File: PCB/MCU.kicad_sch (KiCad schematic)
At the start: 28 parts, among them J1 SWD, SW65 USB Boot, SW66 Reset, U2 W25Q128JVS, U3 RP2040, Y1 12MHz

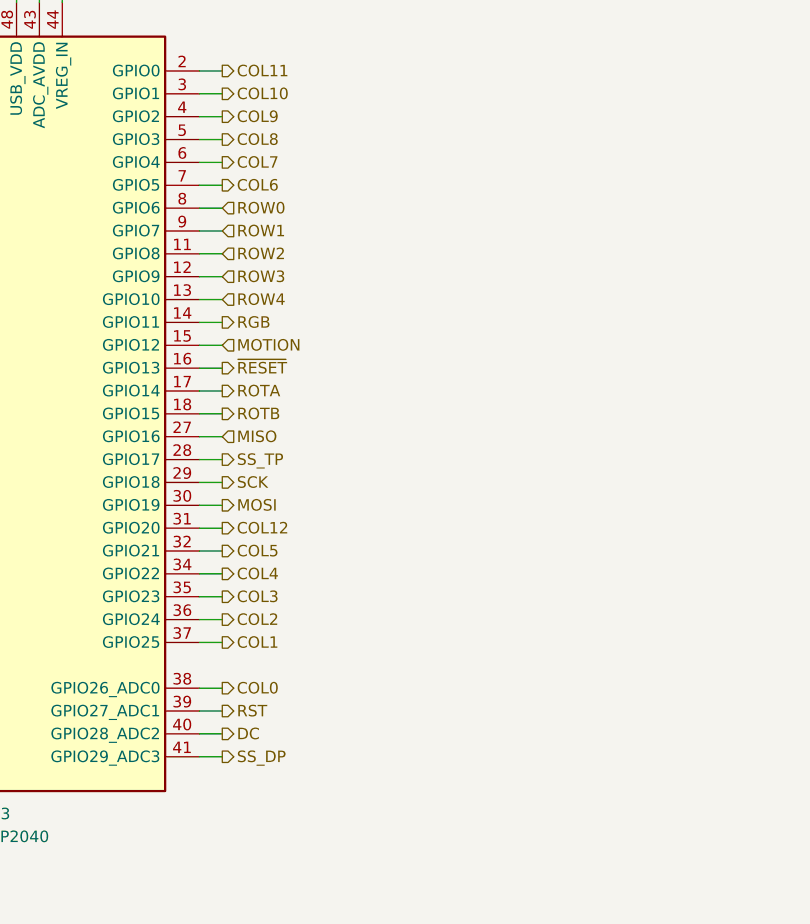
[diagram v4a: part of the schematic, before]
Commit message: Added level shifter to the RGB signal, just in case.
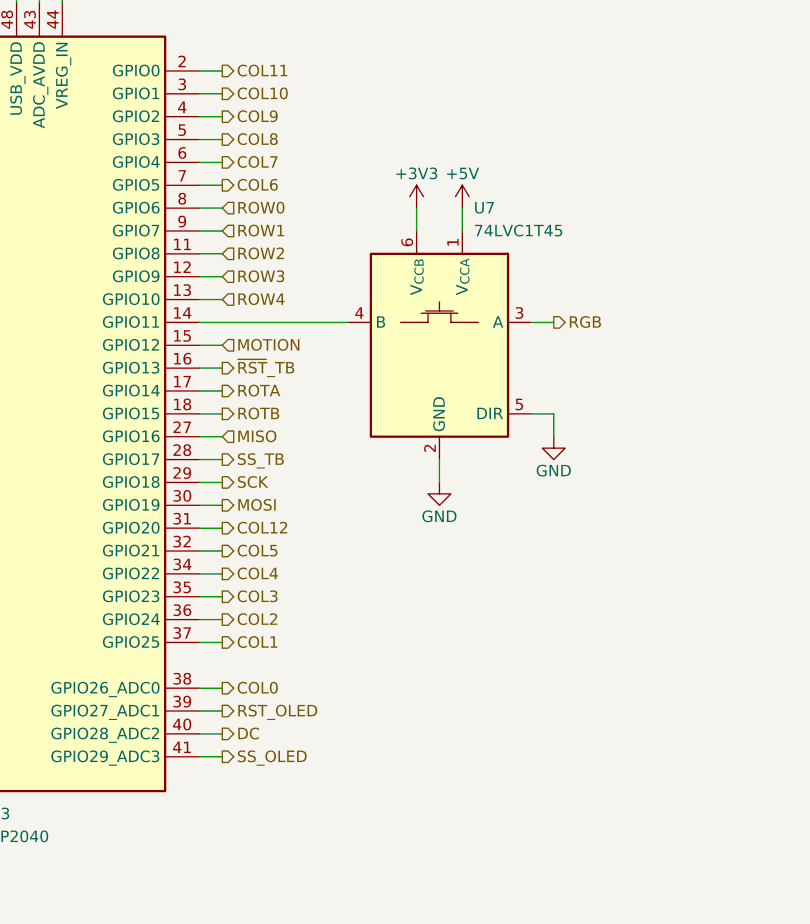
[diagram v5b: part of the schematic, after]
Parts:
- added U7: 74LVC1T45, Package_TO_SOT_SMD:SOT-363_SC-70-6, symbol Cantaloupe:74LVC1T45
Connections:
- net +3V3: now also U7.6 (V_{CCB})
- net GND: now also U7.2 (GND), U7.5 (DIR)
- net RGB: now also U7.3 (A); no longer U3.14 (GPIO11)
- net RST renamed RST_OLED
- net SS_DP renamed SS_OLED
- net SS_TP renamed SS_TB
- net ~{RESET} renamed ~{RST}_TB
- new net: U3.14 (GPIO11), U7.4 (B)
- new net +5V: U7.1 (V_{CCA})
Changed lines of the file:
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@@
 (kicad_sch (version 20230121) (generator eeschema)
   (paper "A4")
+  (title_block
+    (date "2023-03-18")
+    (rev "V1.1")
+  )
   (junction (at 132.08 31.75) (diameter 0) (color 0 0 0 0)
   )
@@
     (stroke (width 0) (type default))
   )
+  (wire (pts (xy 114.3 86.36) (xy 130.81 86.36))
+    (stroke (width 0) (type default))
+  )
   (wire (pts (xy 193.04 31.75) (xy 193.04 34.29))
     (stroke (width 0) (type default))
@@
     (stroke (width 0) (type default))
   )
+  (wire (pts (xy 143.51 73.66) (xy 143.51 76.2))
+    (stroke (width 0) (type default))
+  )
+  (wire (pts (xy 138.43 73.66) (xy 138.43 76.2))
+    (stroke (width 0) (type default))
+  )
   (wire (pts (xy 60.96 129.54) (xy 60.96 127))
     (stroke (width 0) (type default))
@@
     (stroke (width 0) (type default))
   )
+  (wire (pts (xy 153.67 96.52) (xy 151.13 96.52))
+    (stroke (width 0) (type default))
+  )
   (wire (pts (xy 152.4 29.21) (xy 152.4 31.75))
     (stroke (width 0) (type default))
@@
     (stroke (width 0) (type default))
   )
-  (wire (pts (xy 114.3 86.36) (xy 116.84 86.36))
-    (stroke (width 0) (type default))
-  )
   (wire (pts (xy 142.24 31.75) (xy 132.08 31.75))
     (stroke (width 0) (type default))
@@
     (stroke (width 0) (type default))
   )
+  (wire (pts (xy 140.97 101.6) (xy 140.97 104.14))
+    (stroke (width 0) (type default))
+  )
   (wire (pts (xy 45.72 114.3) (xy 48.26 114.3))
     (stroke (width 0) (type default))
@@
     (stroke (width 0) (type default))
   )
+  (wire (pts (xy 151.13 86.36) (xy 153.67 86.36))
+    (stroke (width 0) (type default))
+  )
   (wire (pts (xy 132.08 31.75) (xy 121.92 31.75))
     (stroke (width 0) (type default))
@@
   )
   (wire (pts (xy 162.56 21.59) (xy 162.56 24.13))
+    (stroke (width 0) (type default))
+  )
+  (wire (pts (xy 153.67 99.06) (xy 153.67 96.52))
     (stroke (width 0) (type default))
   )
@@
     (effects (font (size 1.27 1.27)) (justify left))
   )
-  (hierarchical_label "RGB" (shape output) (at 116.84 86.36 0) (fields_autoplaced)
-    (effects (font (size 1.27 1.27)) (justify left))
-  )
   (hierarchical_label "D+" (shape input) (at 53.34 66.04 180) (fields_autoplaced)
     (effects (font (size 1.27 1.27)) (justify right))
   )
-  (hierarchical_label "RST" (shape output) (at 116.84 129.54 0) (fields_autoplaced)
+  (hierarchical_label "SS_TB" (shape output) (at 116.84 101.6 0) (fields_autoplaced)
     (effects (font (size 1.27 1.27)) (justify left))
   )
@@
     (effects (font (size 1.27 1.27)) (justify left))
   )
-  (hierarchical_label "SS_TP" (shape output) (at 116.84 101.6 0) (fields_autoplaced)
-    (effects (font (size 1.27 1.27)) (justify left))
-  )
   (hierarchical_label "ROTB" (shape output) (at 116.84 96.52 0) (fields_autoplaced)
     (effects (font (size 1.27 1.27)) (justify left))
@@
     (effects (font (size 1.27 1.27)) (justify left))
   )
-  (hierarchical_label "~{RESET}" (shape output) (at 116.84 91.44 0) (fields_autoplaced)
-    (effects (font (size 1.27 1.27)) (justify left))
-  )
   (hierarchical_label "ROW4" (shape input) (at 116.84 83.82 0) (fields_autoplaced)
     (effects (font (size 1.27 1.27)) (justify left))
   )
-  (hierarchical_label "SS_DP" (shape output) (at 116.84 134.62 0) (fields_autoplaced)
-    (effects (font (size 1.27 1.27)) (justify left))
-  )
   (hierarchical_label "SCK" (shape output) (at 116.84 104.14 0) (fields_autoplaced)
     (effects (font (size 1.27 1.27)) (justify left))
@@
     (effects (font (size 1.27 1.27)) (justify left))
   )
+  (hierarchical_label "RST_OLED" (shape output) (at 116.84 129.54 0) (fields_autoplaced)
+    (effects (font (size 1.27 1.27)) (justify left))
+  )
   (hierarchical_label "COL12" (shape output) (at 116.84 109.22 0) (fields_autoplaced)
     (effects (font (size 1.27 1.27)) (justify left))
@@
     (effects (font (size 1.27 1.27)) (justify left))
   )
+  (hierarchical_label "RGB" (shape output) (at 153.67 86.36 0) (fields_autoplaced)
+    (effects (font (size 1.27 1.27)) (justify left))
+  )
+  (hierarchical_label "~{RST}_TB" (shape output) (at 116.84 91.44 0) (fields_autoplaced)
+    (effects (font (size 1.27 1.27)) (justify left))
+  )
   (hierarchical_label "COL5" (shape output) (at 116.84 111.76 0) (fields_autoplaced)
+    (effects (font (size 1.27 1.27)) (justify left))
+  )
+  (hierarchical_label "SS_OLED" (shape output) (at 116.84 134.62 0) (fields_autoplaced)
     (effects (font (size 1.27 1.27)) (justify left))
   )
@@
     )
   )
+  (symbol (lib_id "power:GND") (at 140.97 104.14 0) (unit 1)
+    (in_bom yes) (on_board yes) (dnp no)
+    (property "Reference" "#PWR056" (at 140.97 110.49 0)
+      (effects (font (size 1.27 1.27)) hide)
+    )
+    (property "Value" "GND" (at 140.97 107.95 0)
+      (effects (font (size 1.27 1.27)))
+    )
+    (property "Footprint" "" (at 140.97 104.14 0)
+      (effects (font (size 1.27 1.27)) hide)
+    )
+    (property "Datasheet" "" (at 140.97 104.14 0)
+      (effects (font (size 1.27 1.27)) hide)
+    )
+    (pin "1")
+    (instances
+      (project "Honeydew"
+        (path "/534caec7-cf60-4f90-b1ed-42c9d445ef0f/d133c1c6-f35d-4b98-81a0-3607ab1d2de1"
+          (reference "#PWR056") (unit 1)
+        )
+      )
+    )
+  )
   (symbol (lib_id "Connector_Generic:Conn_01x04") (at 50.8 127 180) (unit 1)
     (in_bom no) (on_board yes) (dnp no) (fields_autoplaced)
@@
     )
   )
+  (symbol (lib_id "power:+5V") (at 143.51 73.66 0) (unit 1)
+    (in_bom yes) (on_board yes) (dnp no) (fields_autoplaced)
+    (property "Reference" "#PWR057" (at 143.51 77.47 0)
+      (effects (font (size 1.27 1.27)) hide)
+    )
+    (property "Value" "+5V" (at 143.51 69.85 0)
+      (effects (font (size 1.27 1.27)))
+    )
+    (property "Footprint" "" (at 143.51 73.66 0)
+      (effects (font (size 1.27 1.27)) hide)
+    )
+    (property "Datasheet" "" (at 143.51 73.66 0)
+      (effects (font (size 1.27 1.27)) hide)
+    )
+    (pin "1")
+    (instances
+      (project "Honeydew"
+        (path "/534caec7-cf60-4f90-b1ed-42c9d445ef0f/d133c1c6-f35d-4b98-81a0-3607ab1d2de1"
+          (reference "#PWR057") (unit 1)
+        )
+      )
+    )
+  )
   (symbol (lib_id "Cantaloupe:SW_SPST_Small") (at 55.88 58.42 0) (unit 1)
     (in_bom yes) (on_board yes) (dnp no) (fields_autoplaced)
@@
     )
   )
+  (symbol (lib_id "power:+3V3") (at 138.43 73.66 0) (unit 1)
+    (in_bom yes) (on_board yes) (dnp no) (fields_autoplaced)
+    (property "Reference" "#PWR055" (at 138.43 77.47 0)
+      (effects (font (size 1.27 1.27)) hide)
+    )
+    (property "Value" "+3V3" (at 138.43 69.85 0)
+      (effects (font (size 1.27 1.27)))
+    )
+    (property "Footprint" "" (at 138.43 73.66 0)
+      (effects (font (size 1.27 1.27)) hide)
+    )
+    (property "Datasheet" "" (at 138.43 73.66 0)
+      (effects (font (size 1.27 1.27)) hide)
+    )
+    (pin "1")
+    (instances
+      (project "Honeydew"
+        (path "/534caec7-cf60-4f90-b1ed-42c9d445ef0f/d133c1c6-f35d-4b98-81a0-3607ab1d2de1"
+          (reference "#PWR055") (unit 1)
+        )
+      )
+    )
+  )
   (symbol (lib_id "power:GND") (at 53.34 48.26 0) (unit 1)
     (in_bom yes) (on_board yes) (dnp no)
@@
     )
   )
+  (symbol (lib_id "power:GND") (at 153.67 99.06 0) (unit 1)
+    (in_bom yes) (on_board yes) (dnp no)
+    (property "Reference" "#PWR017" (at 153.67 105.41 0)
+      (effects (font (size 1.27 1.27)) hide)
+    )
+    (property "Value" "GND" (at 153.67 102.87 0)
+      (effects (font (size 1.27 1.27)))
+    )
+    (property "Footprint" "" (at 153.67 99.06 0)
+      (effects (font (size 1.27 1.27)) hide)
+    )
+    (property "Datasheet" "" (at 153.67 99.06 0)
+      (effects (font (size 1.27 1.27)) hide)
+    )
+    (pin "1")
+    (instances
+      (project "Honeydew"
+        (path "/534caec7-cf60-4f90-b1ed-42c9d445ef0f/d133c1c6-f35d-4b98-81a0-3607ab1d2de1"
+          (reference "#PWR017") (unit 1)
+        )
+      )
+    )
+  )
   (symbol (lib_id "Device:C_Small") (at 132.08 26.67 180) (unit 1)
     (in_bom yes) (on_board yes) (dnp no) (fields_autoplaced)
@@
         )
       )
+    )
+  )
+  (symbol (lib_id "Cantaloupe:74LVC1T45") (at 140.97 88.9 0) (mirror y) (unit 1)
+    (in_bom yes) (on_board yes) (dnp no)
+    (property "Reference" "U7" (at 144.78 73.66 0)
+      (effects (font (size 1.27 1.27)) (justify right))
+    )
+    (property "Value" "74LVC1T45" (at 144.78 76.2 0)
+      (effects (font (size 1.27 1.27)) (justify right))
+    )
+    (property "Footprint" "Package_TO_SOT_SMD:SOT-363_SC-70-6" (at 139.7 97.79 0)
+      (effects (font (size 1.27 1.27)) (justify left) hide)
+    )
+    (property "Datasheet" "https://www.ti.com/lit/ds/symlink/sn74lvc1t45.pdf" (at 140.97 110.49 0)
+      (effects (font (size 1.27 1.27)) hide)
+    )
+    (property "LCSC" "C168855" (at 140.97 88.9 0)
+      (effects (font (size 1.27 1.27)) hide)
+    )
+    (pin "1")
+    (pin "2")
+    (pin "3")
+    (pin "4")
+    (pin "5")
+    (pin "6")
+    (instances
+      (project "Honeydew"
+        (path "/534caec7-cf60-4f90-b1ed-42c9d445ef0f/d133c1c6-f35d-4b98-81a0-3607ab1d2de1"
+          (reference "U7") (unit 1)
+        )
+      )

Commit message: More V1.1 updates
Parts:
- J1: footprint Connector_PinHeader_2.54mm:PinHeader_1x04_P2.54mm_Vertical -> Honeydew:PinHeader_1x04_P2.54mm_Vertical_SIlkless
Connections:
- net ~{RST}: now reaches R10.1, SW66.2 (B), U3.26 (RUN)
- net DC renamed DC_OLED
- net RST_OLED: no longer names the net of U3.39 (GPIO27_ADC1)
- net ~{RST}_TB renamed ROTC
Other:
- moved on the sheet: R10, SW66, U7

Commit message: Initial V2.0 update.
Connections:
- net ROTC is gone; now on net MOTION: U3.16 (GPIO13)
- net COL0: now also U3.37 (GPIO25); no longer U3.38 (GPIO26_ADC0)
- net COL1: now also U3.36 (GPIO24); no longer U3.37 (GPIO25)
- net COL12: now also U3.14 (GPIO11); no longer U3.31 (GPIO20)
- net COL2: now also U3.35 (GPIO23); no longer U3.36 (GPIO24)
- net COL3: now also U3.34 (GPIO22); no longer U3.35 (GPIO23)
- net COL4: now also U3.32 (GPIO21); no longer U3.34 (GPIO22)
- net COL5: now also U3.31 (GPIO20); no longer U3.32 (GPIO21)
- net MOTION: no longer U3.15 (GPIO12)
- net at U7.4 (B): now also U3.15 (GPIO12); no longer U3.14 (GPIO11)
- net TX: now reaches U3.39 (GPIO27_ADC1)
- new net RX: U3.38 (GPIO26_ADC0)
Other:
- moved on the sheet: U7

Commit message: Additional changes.
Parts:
- removed R10: 10k, Resistor_SMD:R_0402_1005Metric, symbol Device:R_Small
- removed SW65: USB Boot, Button_Switch_SMD:SW_DIP_SPSTx01_Slide_6.7x4.1mm_W8.61mm_P2.54mm_LowProfile, symbol Switch:SW_DIP_x01
- removed U7: 74LVC1T45, Package_TO_SOT_SMD:SOT-363_SC-70-6, symbol Cantaloupe:74LVC1T45
- added C93: 10u, Capacitor_SMD:C_0603_1608Metric, symbol Device:C_Small
- added C98: 100n, Capacitor_SMD:C_0402_1005Metric, symbol Device:C_Small
- added D63: 1N4148, Honeydew:D_SOD-323, symbol Device:D_Small
- added Q7, Q8, Q9: 2N7002, Package_TO_SOT_SMD:SOT-23, symbol Transistor_FET:2N7002
- added R10: 100k, Resistor_SMD:R_0402_1005Metric, symbol Device:R_Small
- added R10 (x3): 10k, Resistor_SMD:R_0402_1005Metric, symbol Device:R_Small
- added R15: 1M, Resistor_SMD:R_0402_1005Metric, symbol Device:R_Small
- added R20: 1k, Resistor_SMD:R_0402_1005Metric, symbol Device:R_Small
- added R21: 120k, Resistor_SMD:R_0402_1005Metric, symbol Device:R_Small
- added U7: SN74AHCT1G125, Package_TO_SOT_SMD:SOT-23-5, symbol Honeydew:SN74AHCT1G125
- R5: now in the parts list
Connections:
- net +3V3: now also R6.1, SW66.2 (B)
- net +5V: now also U7.5 (VCC)
- net GND: now also C93.1, C98.1, Q7.2 (S), Q8.2 (S), Q9.2 (S), R10.1, R10.2, R15.1, U7.1 (~{OE}), U7.3 (GND); no longer SW66.1 (A)
- net RGB: now also U7.4 (Y)
- net ~{RST}: now also R6.2, C98.2, Q7.3 (D), R10.2; no longer SW66.2 (B)
- net Flash_SS: now reaches R5.1, U2.1 (~{CS}), U3.56 (QSPI_SS)
- net Flash_SS: now also Q9.3 (D); no longer R6.2
- net at U3.15 (GPIO12): now also U7.2 (A)
- new net: Q7.1 (G), R10.2, R20.1
- new net: Q8.1 (G), R10.1, R10.1
- new net: C93.2, Q9.1 (G), R10.2, R15.2, R21.1
- new net: Q8.3 (D), R10.1
- new net: D63.2 (A), R20.2, SW66.1 (A)
- new net: D63.1 (K), R21.2
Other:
- moved on the sheet: C10, C11, C12, C13, C14, C15, C16, C17, C18, C19, C5, C6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
